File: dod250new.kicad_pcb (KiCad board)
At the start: 2 copper layers, 52 x 100 mm, 32 parts, among them J1 Barrel_Jack_Switch, J2 NRJ4HF-1, J3 NRJ4HF, SW1 SW_FSW800_3PDT, U1 TL071

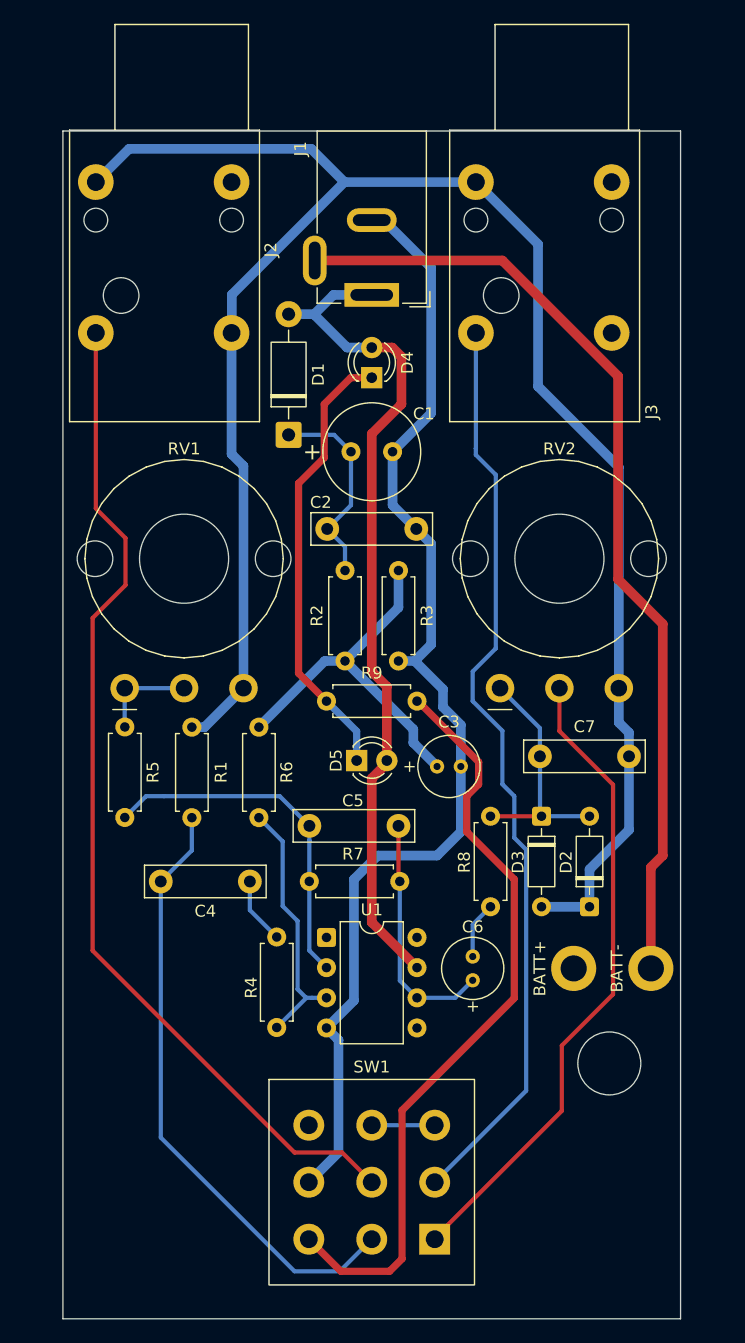
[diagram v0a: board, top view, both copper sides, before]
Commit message: v1.1 sent to JLCPC 6/4/26 evening -- resolved 9V0 battery net disconnect
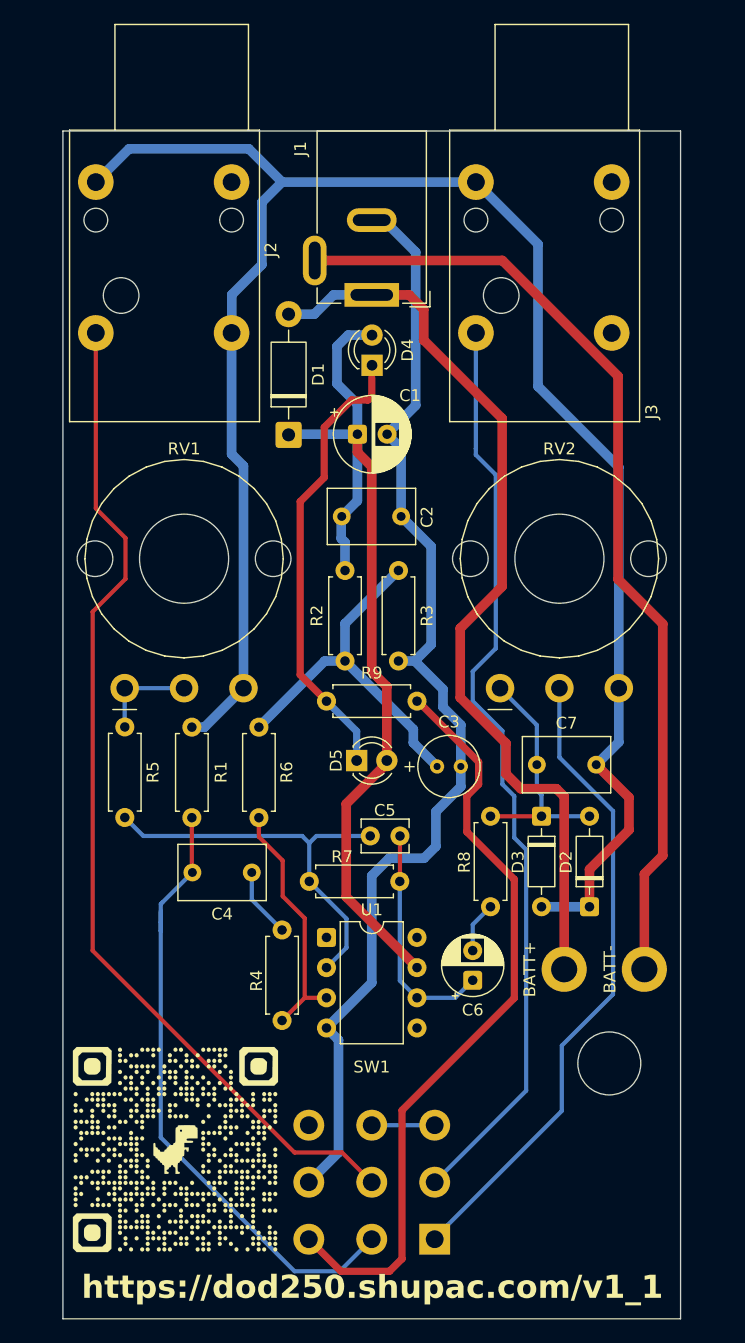
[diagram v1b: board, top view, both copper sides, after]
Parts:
- removed BATT+, BATT-: MountingHole_Pad, MountingHole:MountingHole_2.2mm_M2_DIN965_Pad
- added H2: BATT+, MountingHole:MountingHole_2.2mm_M2_DIN965_Pad, F.Cu at (146.7, 130.1)
- added H3: BATT-, MountingHole:MountingHole_2.2mm_M2_DIN965_Pad, F.Cu at (153.4, 130.1)
- C1: footprint Capacitor_THT:C_Radial_D8.0mm_H11.5mm_P3.50mm -> Capacitor_THT:CP_Radial_D6.3mm_P2.50mm
- C2, C4, C7: footprint Capacitor_THT:C_Rect_L10.0mm_W2.5mm_P7.50mm_MKS4 -> Capacitor_THT:C_Rect_L7.2mm_W4.5mm_P5.00mm
- C5: footprint Capacitor_THT:C_Rect_L10.0mm_W2.5mm_P7.50mm_MKS4 -> Capacitor_THT:C_Disc_D3.8mm_W2.6mm_P2.50mm
- C6: footprint Capacitor_THT:C_Radial_D5.0mm_H7.0mm_P2.00mm -> Capacitor_THT:CP_Radial_D5.0mm_P2.50mm
- G***: moved to F.Cu
- moved G*** 33.4 mm to (114.0, 145.2), turned to 0 degrees
- moved C2 1.61 mm to (128.0, 92.0)
- moved C1 1.57 mm to (129.3, 85.0)
- moved D4 1.05 mm to (130.5, 79.2)
- moved C5 0.86 mm to (132.9, 118.8)
- moved C4 0.77 mm to (120.4, 121.9)
- moved C7 0.75 mm to (144.4, 112.8)
- moved R4 0.74 mm to (123.0, 126.8)
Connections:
- C1 pad 1: Net-(D1-K) -> /9V0
- C2 pad 1: Net-(D1-K) -> /9V0
- D1 pad 1: Net-(D1-K) -> /9V0
- D1 pad 2: /9V0 -> /9V0_RAW
- J1 pad 1: /9V0 -> /9V0_RAW
- R2 pad 2: Net-(D1-K) -> /9V0
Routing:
- net /9V0_RAW: track 0.00 -> 77.7 mm
- net Net-(D1-K): track 17.3 -> 0.00 mm
- net /9V0: track 71.8 -> 79.5 mm
- net /INV: track 28.9 -> 34.3 mm
- net /PGND: track 99.0 -> 97.1 mm
- net /CIRCIN: track 51.6 -> 53.2 mm
- net /OPAMPOUT: track 20.4 -> 19.5 mm
- net /NINV: track 22.1 -> 21.3 mm
- net /AGND: track 158.7 -> 158.1 mm
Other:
- board text added: "https://dod250.shupac.com/v1_1"
- board text added: "v1.1"
